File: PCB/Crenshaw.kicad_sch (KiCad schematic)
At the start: 7 parts, among them J1 In, J6 Out

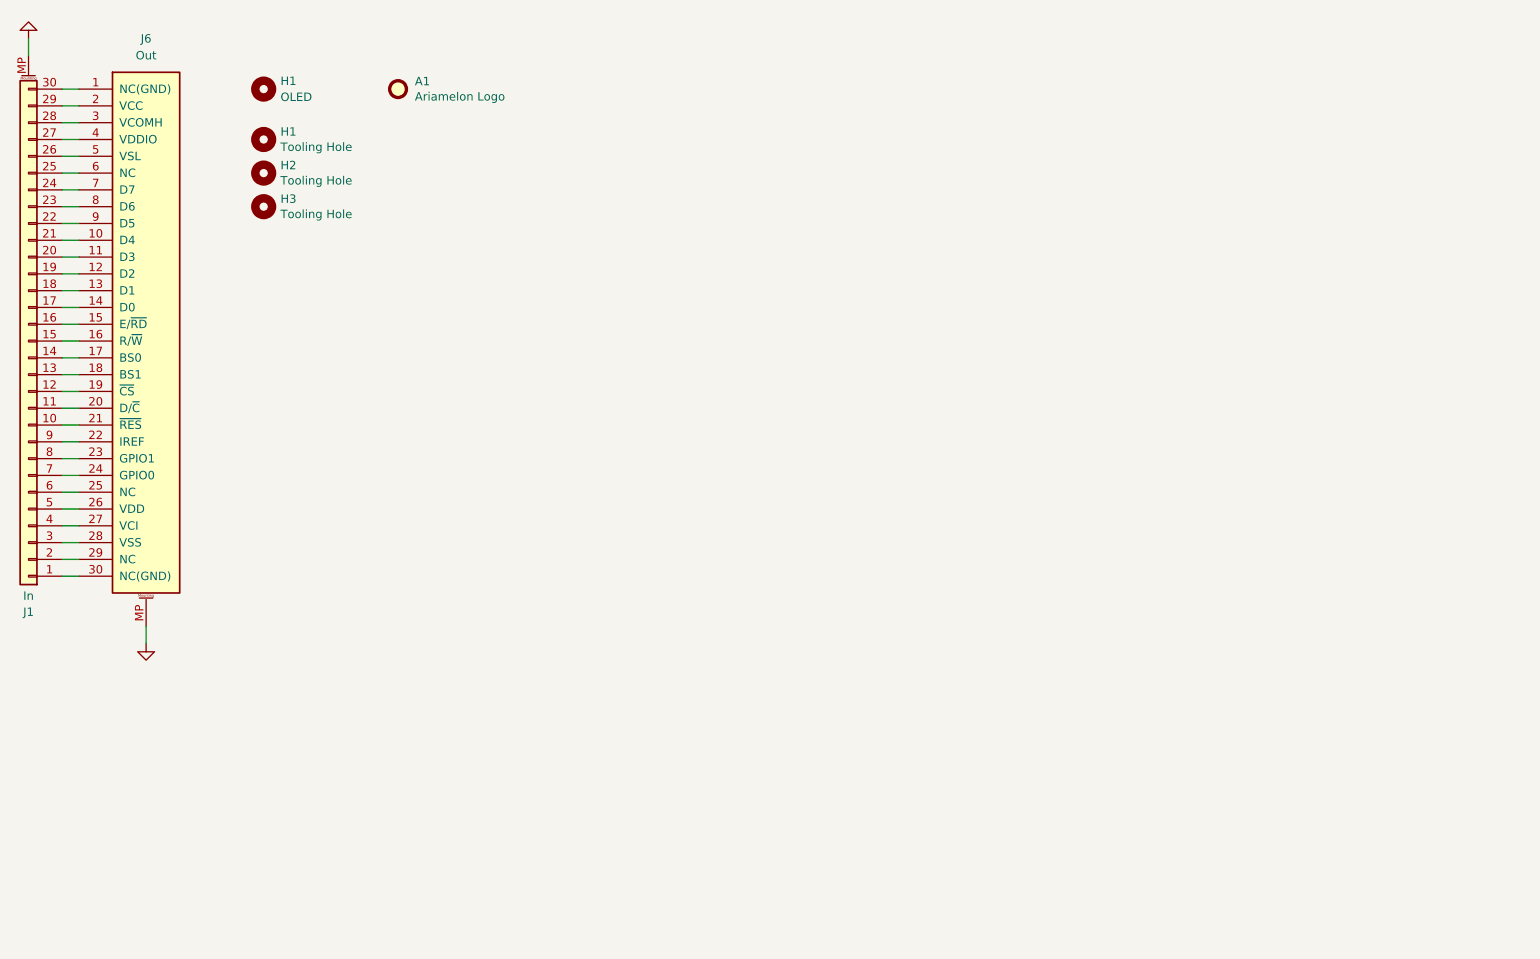
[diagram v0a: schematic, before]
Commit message: 27/03/2023 update
Added voltage regulator, SSD1351 supporting circuitry and [VIK](https://github.com/sadekbaroudi/vik) connector. Added license. Added metadata to schematic and board files. Added VIK module certification card.
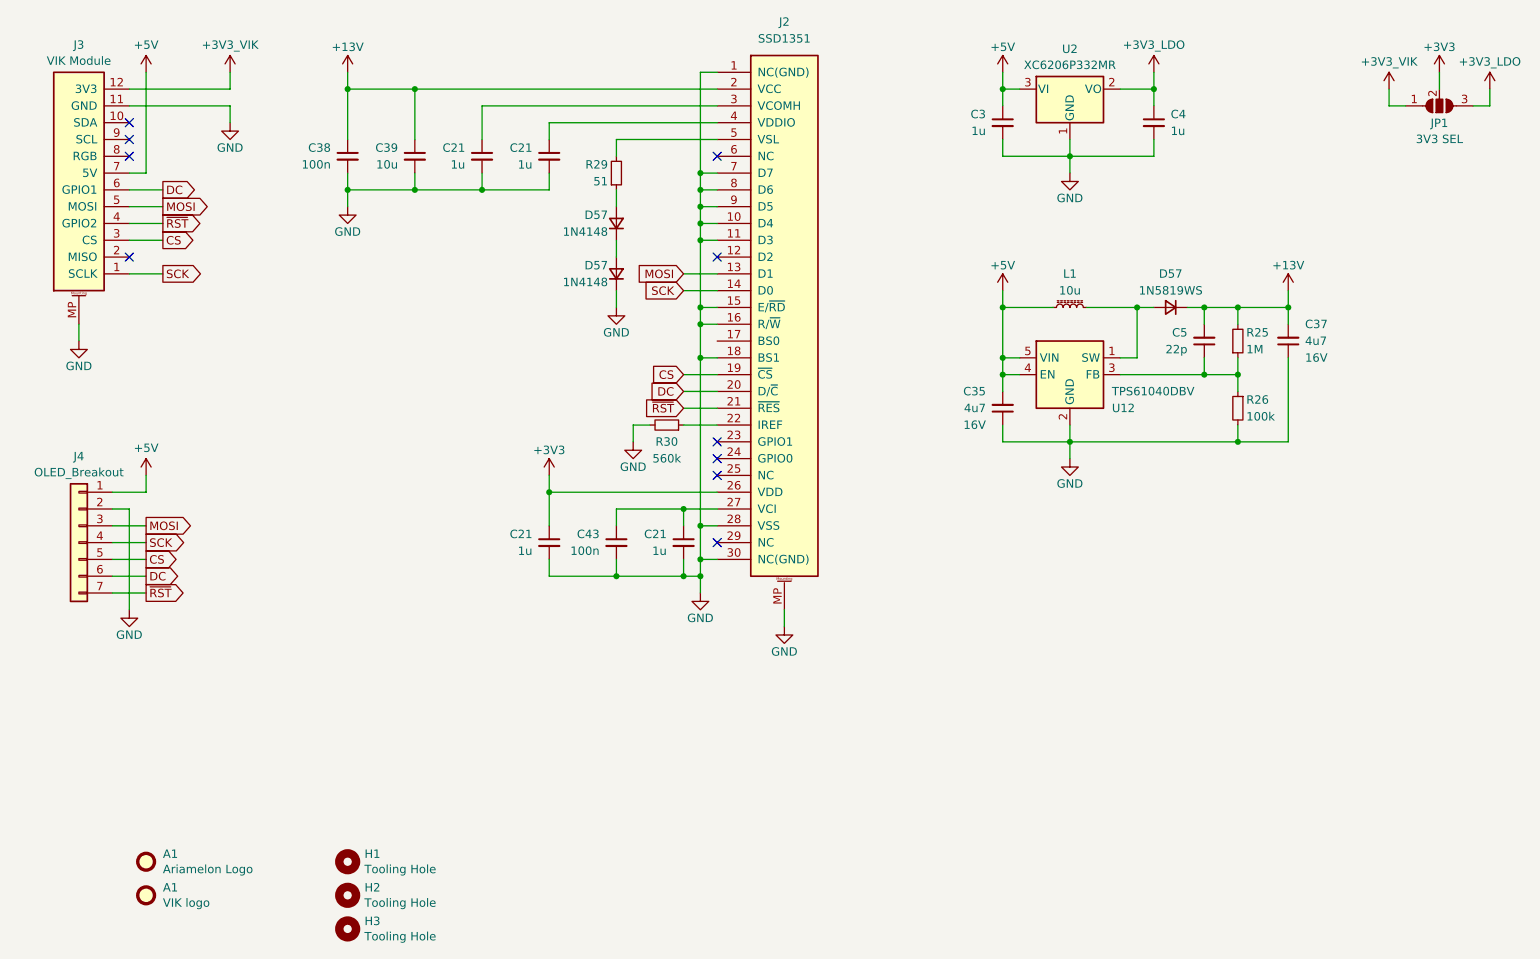
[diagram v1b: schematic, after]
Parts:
- removed H1: OLED, Crenshaw:OLED_1.5_SSD1351_128x128_NoHoles, symbol Mechanical:MountingHole
- removed J1: In, Crenshaw:HRS_FH34SRJ-30S-0.5SH(50), symbol Connector_Generic_MountingPin:Conn_01x30_MountingPin
- removed J6: Out, Crenshaw:HRS_FH34SRJ-30S-0.5SH(50), symbol Honeydew:SSD1351
- added A1: VIK logo, Crenshaw:vik-logo-small, symbol Mechanical:Fiducial
- added C21 (x4): 1u, Capacitor_SMD:C_0603_1608Metric, symbol Device:C_Small
- added C3, C4: 1u, Capacitor_SMD:C_0402_1005Metric, symbol Device:C_Small
- added C35, C37: 4u7, Capacitor_SMD:C_0603_1608Metric, symbol Device:C_Small
- added C38, C43: 100n, Capacitor_SMD:C_0402_1005Metric, symbol Device:C_Small
- added C39: 10u, Capacitor_SMD:C_0603_1608Metric, symbol Device:C_Small
- added C5: 22p, Capacitor_SMD:C_0402_1005Metric, symbol Device:C_Small
- added D57 (x2): 1N4148, Diode_SMD:D_SOD-323, symbol Device:D_Small
- added D57: 1N5819WS, Diode_SMD:D_SOD-323, symbol Device:D_Small
- added J2: SSD1351, Crenshaw:HRS_FH34SRJ-30S-0.5SH(50), symbol Crenshaw:SSD1351
- added J3: VIK Module, Crenshaw:vik-module-connector-horizontal, symbol Crenshaw:vik-module-connector
- added J4: OLED_Breakout, Crenshaw:OLED_1.5_SSD1351_128x128, symbol Connector_Generic:Conn_01x07
- added JP1: 3V3 SEL, Jumper:SolderJumper-3_P1.3mm_Open_Pad1.0x1.5mm_NumberLabels, symbol Crenshaw:SolderJumper_3_Open
- added L1: 10u, Inductor_SMD:L_Sunlord_SWPA3012S, symbol Device:L_Ferrite_Small
- added R25: 1M, Resistor_SMD:R_0402_1005Metric, symbol Device:R_Small
- added R26: 100k, Resistor_SMD:R_0402_1005Metric, symbol Device:R_Small
- added R29: 51, Resistor_SMD:R_0402_1005Metric, symbol Device:R_Small
- added R30: 560k, Resistor_SMD:R_0603_1608Metric, symbol Device:R_Small
- added U12: TPS61040DBV, Package_TO_SOT_SMD:SOT-23-5, symbol Regulator_Switching:TPS61040DBV
- added U2: XC6206P332MR, Package_TO_SOT_SMD:SOT-23, symbol Regulator_Linear:XC6206PxxxMR
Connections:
- net GND: now also C21.2, C21.2, C21.2, C21.2, C3.2, C35.1, C37.1, C38.2, C39.2, C4.2, C43.2, D57.1 (K), J2.1 (NC(GND)), J2.10 (D4), J2.11 (D3), J2.15 (E/~{RD}), J2.16 (R/~{W}), J2.18 (BS1), J2.28 (VSS), J2.30 (NC(GND)), J2.7 (D7), J2.8 (D6), J2.9 (D5), J2.MP, J3.11 (GND), J3.MP, J4.2 (Pin_2), R26.2, R30.2, U12.2 (GND), U2.1 (GND)
- new net: D57.1 (K), D57.2 (A)
- new net: C21.1, C43.1, J2.27 (VCI)
- new net: D57.2 (A), L1.1, U12.1 (SW)
- new net: C5.1, R25.1, R26.1, U12.3 (FB)
- new net: D57.2 (A), R29.1
- new net: J2.5 (VSL), R29.2
- new net: C21.1, J2.3 (VCOMH)
- new net: C21.1, J2.4 (VDDIO)
- new net: J2.22 (IREF), R30.1
- new net +13V: C37.2, C38.1, C39.1, C5.2, D57.1 (K), J2.2 (VCC), R25.2
- new net +3V3: C21.1, J2.26 (VDD), JP1.2 (C)
- new net +3V3_LDO: C4.1, JP1.3 (B), U2.2 (VO)
- new net +3V3_VIK: J3.12 (3V3), JP1.1 (A)
- new net +5V: C3.1, C35.2, J3.7 (5V), J4.1 (Pin_1), L1.2, U12.4 (EN), U12.5 (VIN), U2.3 (VI)
- new net CS: J2.19 (~{CS}), J3.3 (CS), J4.5 (Pin_5)
- new net DC: J2.20 (D/~{C}), J3.6 (GPIO1), J4.6 (Pin_6)
- new net MOSI: J2.13 (D1), J3.5 (MOSI), J4.3 (Pin_3)
- new net SCK: J2.14 (D0), J3.1 (SCLK), J4.4 (Pin_4)
- new net ~{RST}: J2.21 (~{RES}), J3.4 (GPIO2), J4.7 (Pin_7)
- no-connect marks 0 -> 10
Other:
- company: (none) -> Created by Ariamelon (https://github.com/Ariamelon/Crenshaw/)
- title: (none) -> Crenshaw SSD1351 OLED breakout
- moved on the sheet: A1, H1, H2, H3

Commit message: 04/08/2023 update
Changed VIK and OLED FFC to FH12. Stitched ground planes together. Fixed VIK footprint. Moved production files to easier to access location.
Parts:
- A1: footprint Crenshaw:Ariamelon_Logo_x3_CU -> Crenshaw:Ariamelon_Logo_x2_Mask
- J2: footprint Crenshaw:HRS_FH34SRJ-30S-0.5SH(50) -> Crenshaw:Hirose_FH12-30S-0.5SH_1x30-1MP_P0.50mm_Horizontal; LCSC C324727 -> C506793
- J3: LCSC C424659 -> C88360
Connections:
- net +13V: now also J2.29 (VCC); no longer J2.2 (VCC)
- net +3V3: now also J2.5 (VDD); no longer J2.26 (VDD)
- net CS: now also J2.12 (~{CS}); no longer J2.19 (~{CS})
- net DC: now also J2.11 (D/~{C}); no longer J2.20 (D/~{C})
- net GND: now also J2.13 (BS1), J2.20 (D3), J2.21 (D4), J2.22 (D5), J2.23 (D6), J2.24 (D7), J2.3 (VSS); no longer J2.10 (D4), J2.11 (D3), J2.18 (BS1), J2.28 (VSS), J2.7 (D7), J2.8 (D6), J2.9 (D5)
- net MOSI: now also J2.18 (D1); no longer J2.13 (D1)
- net SCK: now also J2.17 (D0); no longer J2.14 (D0)
- net ~{RST}: now also J2.10 (~{RES}); no longer J2.21 (~{RES})
- net at C21.1, C43.1: now also J2.4 (VCI); no longer J2.27 (VCI)
- net at R29.2: now also J2.26 (VSL); no longer J2.5 (VSL)
- net at C21.1: now also J2.28 (VCOMH); no longer J2.3 (VCOMH)
- net at C21.1: now also J2.27 (VDDIO); no longer J2.4 (VDDIO)
- net at R30.1: now also J2.9 (IREF); no longer J2.22 (IREF)
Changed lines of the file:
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@@
       (effects (font (size 1.27 1.27)) (justify left))
     )
-    (property "Footprint" "Crenshaw:Ariamelon_Logo_x3_CU" (at 35.56 142.24 0)
+    (property "Footprint" "Crenshaw:Ariamelon_Logo_x2_Mask" (at 35.56 142.24 0)
       (effects (font (size 1.27 1.27)) hide)
     )
@@
       (effects (font (size 1.27 1.27)) hide)
     )
-    (property "LCSC" "C424659" (at 25.4 38.1 0)
+    (property "LCSC" "C88360" (at 25.4 38.1 0)
       (effects (font (size 1.27 1.27)) hide)
     )
@@
       (effects (font (size 1.27 1.27)))
     )
-    (property "Footprint" "Crenshaw:HRS_FH34SRJ-30S-0.5SH(50)" (at 128.27 58.42 0)
+    (property "Footprint" "Crenshaw:Hirose_FH12-30S-0.5SH_1x30-1MP_P0.50mm_Horizontal" (at 128.27 58.42 0)
       (effects (font (size 1.27 1.27)) hide)
     )
@@
       (effects (font (size 1.27 1.27)) hide)
     )
-    (property "LCSC" "C324727" (at 132.08 58.42 0)
-      (effects (font (size 1.27 1.27)) hide)
-    )
+    (property "LCSC" "C506793" (at 132.08 58.42 0)
+      (effects (font (size 1.27 1.27)) hide)
+    )
